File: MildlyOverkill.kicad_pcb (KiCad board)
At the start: 4 copper layers, 195 x 124 mm, 149 parts, among them J1 USB_C_Receptacle_USB2.0_16P, J2 2604-1102, J3 2604-1104, J4 2604-1104, J5 Conn_01x04_Pin, J6 Conn_01x04_MountingPin, J7 Conn_01x04_Pin, Q10 BTN8982TA, Q5 QM6015D, Q7 BTN8982TA, Q8 BTN8982TA, Q9 BTN8982TA, U1 ESP32-S3-WROOM-1, U2 MCP3208, U3 LD1117S33TR_SOT223, U4 TPS4H160AQPWPRQ1, U5 USBLC6-2P6, U6 TPS62932

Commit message: Added ethernet and ntcs
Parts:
- added C15: 1.5nF, Capacitor_SMD:C_0603_1608Metric, F.Cu at (27.5, 125.4)
- added C18: 1.5nF, Capacitor_SMD:C_0603_1608Metric, F.Cu at (39.5, 125.4)
- added C19: 1.5nF, Capacitor_SMD:C_0603_1608Metric, F.Cu at (33.5, 125.4)
- added C20: 1.5nF, Capacitor_SMD:C_0603_1608Metric, F.Cu at (45.5, 125.4)
- added J8: RJ45_Wuerth_7499010211A, Connector_RJ:RJ45_Wuerth_7499010211A_Horizontal, F.Cu at (163.2, 59.4)
- added TH1: Thermistor_NTC, Resistor_SMD:R_0805_2012Metric_Pad1.20x1.40mm_HandSolder, F.Cu at (27.9, 114.8)
- added TH2: Thermistor_NTC, Resistor_SMD:R_0805_2012Metric_Pad1.20x1.40mm_HandSolder, F.Cu at (27.9, 117.7)
- added TH3: Thermistor_NTC, Resistor_SMD:R_0805_2012Metric_Pad1.20x1.40mm_HandSolder, F.Cu at (27.9, 120.7)
- added U7: W5500, Package_QFP:LQFP-48_7x7mm_P0.5mm, F.Cu at (158.5, 75.5)
- R14, R23, R8, R9: value 6k -> 33k
- R25, R26, R27, R28: value 3k -> 3.3k
- R57, R58, R59, R60: value 5.1k -> 0R; footprint Resistor_SMD:R_0805_2012Metric -> Resistor_SMD:R_0805_2012Metric_Pad1.20x1.40mm_HandSolder
- R64, R65, R67, R68, R69, R70, R71, R72: footprint Resistor_SMD:R_0603_1608Metric_Pad0.98x0.95mm_HandSolder -> Resistor_SMD:R_0805_2012Metric_Pad1.20x1.40mm_HandSolder
- moved J2 168.8 mm to (251.5, 54.2), turned to 180 degrees
- moved C16 155.5 mm to (255.0, 75.5)
- moved C10 133.3 mm to (55.5, 67.7)
- moved C11 133.3 mm to (48.5, 95.0)
- moved C12 133.3 mm to (52.0, 71.7)
- moved C13 133.3 mm to (45.5, 74.5)
- moved C14 133.3 mm to (41.5, 75.5)
- moved C5 133.3 mm to (57.0, 73.5)
- moved L1 133.3 mm to (56.5, 84.0)
- moved R55 133.3 mm to (53.5, 67.6)
- moved R56 133.3 mm to (51.5, 67.6)
- moved U6 133.3 mm to (48.5, 73.0)
- moved D22 110.1 mm to (51.5, 101.7), turned to 90 degrees
- moved J6 58.3 mm to (115.7, 74.7)
- moved U4 53.5 mm to (150.3, 130.8)
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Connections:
- D11 pad 1: Net-(D11-K) -> GND
- D11 pad 2: GND -> Net-(D11-A)
- D12 pad 1: Net-(D12-K) -> GND
- D12 pad 2: GND -> Net-(D12-A)
- D13 pad 1: Net-(D13-K) -> GND
- D13 pad 2: GND -> Net-(D13-A)
- D23 pad 1: Net-(D23-K) -> GND
- D23 pad 2: GND -> Net-(D23-A)
- R14 pad 2: Net-(D3-K) -> GPIO3
- R23 pad 2: Net-(D4-K) -> GPIO4
- R25 pad 1: Net-(D1-K) -> GPIO1
- R26 pad 1: Net-(D2-K) -> GPIO2
- R27 pad 1: Net-(D3-K) -> GPIO3
- R28 pad 1: Net-(D4-K) -> GPIO4
- R52 pad 2: Net-(D11-K) -> Net-(D11-A)
- R53 pad 2: Net-(D12-K) -> Net-(D12-A)
- R54 pad 2: Net-(D13-K) -> Net-(D13-A)
- R61 pad 2: Net-(D23-K) -> Net-(D23-A)
- R8 pad 2: Net-(D1-K) -> GPIO1
- R9 pad 2: Net-(D2-K) -> GPIO2
- U1 pad 31: LED2 -> ETH_CS
- U2 pad 5: unconnected-(U2-CH4-Pad5) -> NTC1
- U2 pad 6: unconnected-(U2-CH5-Pad6) -> NTC2
- U2 pad 7: unconnected-(U2-CH6-Pad7) -> NTC3
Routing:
- added copper zone on F.Cu, net GPIO1
- added copper zone on F.Cu, net GPIO2
- added copper zone on F.Cu, net GPIO3
- added copper zone on F.Cu, net GPIO4
- removed copper zone on F.Cu, net Net-(D1-K)
- removed copper zone on F.Cu, net Net-(D2-K)
- removed copper zone on F.Cu, net Net-(D3-K)
- removed copper zone on F.Cu, net Net-(D4-K)

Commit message: kinda finished high power i guess
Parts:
- removed D1, D2, D3, D4: 3v, Diode_SMD:D_SOD-123
- removed D24: 5V, LED_SMD:LED_0603_1608Metric
- added C21: 0.1uF, Capacitor_SMD:C_0603_1608Metric, F.Cu at (41.0, 3.27)
- added C26: 10uF 16V, Capacitor_THT:CP_Radial_D4.0mm_P2.00mm, F.Cu at (32.6, 16.5)
- added C27: 4.7uF, Capacitor_SMD:C_1206_3216Metric, F.Cu at (41.4, 46.8)
- added C28: 10nF, Capacitor_SMD:C_0805_2012Metric, F.Cu at (36.3, 26.6)
- added C29: 10nF, Capacitor_SMD:C_0805_2012Metric, F.Cu at (36.3, 29.6)
- added C30: 10nF, Capacitor_SMD:C_0805_2012Metric, F.Cu at (36.3, 32.6)
- added C31: 10nF, Capacitor_SMD:C_0805_2012Metric, F.Cu at (36.3, 35.6)
- added C32: 22nF, Capacitor_SMD:C_0805_2012Metric, F.Cu at (36.3, 38.6)
- added C33: 18pF, Capacitor_SMD:C_0805_2012Metric, F.Cu at (36.3, 41.7)
- added C34: 18pF, Capacitor_SMD:C_0805_2012Metric, F.Cu at (36.3, 44.7)
- added C35: 10uF 16V, Capacitor_THT:CP_Radial_D4.0mm_P2.00mm, F.Cu at (20.5, 52.0)
- added C36: 0.1uF, Capacitor_SMD:C_0603_1608Metric, F.Cu at (40.5, 62.0)
- added C37: 0.1uF, Capacitor_SMD:C_0603_1608Metric, F.Cu at (40.5, 64.5)
- added C38: 0.1uF, Capacitor_SMD:C_0603_1608Metric, F.Cu at (40.5, 67.0)
- added C39: 0.1uF, Capacitor_SMD:C_0603_1608Metric, F.Cu at (44.5, 57.0)
- added C40: 0.1uF, Capacitor_SMD:C_0603_1608Metric, F.Cu at (48.4, 59.7)
- added C41: 0.1uF, Capacitor_SMD:C_0603_1608Metric, F.Cu at (44.5, 62.0)
- added C42: 1nF 10kV, Capacitor_SMD:C_0805_2012Metric, F.Cu at (36.3, 47.7)
- added FB2: GZ2012D121TF, Inductor_SMD:L_0805_2012Metric, F.Cu at (2.27, 61.0)
- added H1: MountingHole, MountingHole:MountingHole_2.1mm, F.Cu at (183.5, 91.5)
- added H2: MountingHole, MountingHole:MountingHole_2.1mm, F.Cu at (258.2, 91.5)
- added H3: MountingHole, MountingHole:MountingHole_2.1mm, F.Cu at (258.2, 147.5)
- added H4: MountingHole, MountingHole:MountingHole_2.1mm, F.Cu at (183.5, 147.5)
- added M1: Fan_4pin, Connector:FanPinHeader_1x04_P2.54mm_Vertical, F.Cu at (143.0, 89.0)
- added R66: 10, Resistor_SMD:R_0805_2012Metric, F.Cu at (6.12, 36.1)
- added R73: 1M, Resistor_SMD:R_0805_2012Metric, F.Cu at (6.12, 39.0)
- added R74: 0, Capacitor_SMD:C_0603_1608Metric_Pad1.08x0.95mm_HandSolder, F.Cu at (6.92, 50.8)
- added R75: 330, Resistor_SMD:R_0805_2012Metric, F.Cu at (6.12, 42.0)
- added R76: 330, Resistor_SMD:R_0805_2012Metric, F.Cu at (10.5, 24.3)
- added R77: R, Resistor_SMD:R_0805_2012Metric, F.Cu at (250.2, 56.5)
- added R78: R, Resistor_SMD:R_0805_2012Metric, F.Cu at (250.2, 54.5)
- added R79: R, Resistor_SMD:R_0805_2012Metric, F.Cu at (250.2, 52.5)
- added Y1: 3134250001, Crystal:Crystal_SMD_3225-4Pin_3.2x2.5mm_HandSoldering, F.Cu at (41.9, 42.2)
- J7: value Conn_01x04_Pin -> Conn_01x02_Pin; footprint Connector_PinHeader_2.54mm:PinHeader_1x04_P2.54mm_Vertical -> Connector_PinHeader_2.54mm:PinHeader_1x02_P2.54mm_Vertical
- R40: value 10K -> 22K
- R41: value 1k -> 12.4K
- R42, R43: value 1k -> 82
- R44: value 1k -> 49
- R49: value 10K -> 39K
- R50: value 10K -> 82K
- R62: value 210 -> 49
- TH2: footprint Resistor_SMD:R_0805_2012Metric_Pad1.20x1.40mm_HandSolder -> Connector_PinHeader_2.54mm:PinHeader_1x02_P2.54mm_Vertical
- moved R42 280.4 mm to (1.71, 27.2), turned to 0 degrees
- moved R44 263.2 mm to (1.71, 33.1), turned to 0 degrees
- moved J4 255.7 mm to (-14.5, -51.7)
- moved C18 228.6 mm to (268.0, 133.3), turned to 180 degrees
- moved C20 222.8 mm to (268.0, 113.3), turned to 180 degrees
- moved R72 213.9 mm to (15.1, 33.1)
- moved R69 213.6 mm to (15.1, 27.2)
- moved R70 213.5 mm to (15.1, 30.2)
- moved R65 212.9 mm to (15.1, 24.3)
- moved TH1 208.9 mm to (234.0, 81.0), turned to 90 degrees
- moved R43 198.0 mm to (1.71, 30.2), turned to 0 degrees
- moved R41 195.6 mm to (1.71, 24.3), turned to 0 degrees
- moved JP9 182.5 mm to (42.0, 37.6)
- moved JP6 181.7 mm to (42.0, 30.5)
- moved JP7 181.7 mm to (42.0, 34.0)
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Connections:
- R40 pad 1: ~{ST2} -> Net-(U4-~{ST2})
- R40 pad 2: +3.3V -> ST
- R41 pad 1: Net-(D1-K) -> Net-(U7-EXRES1)
- R41 pad 2: GPIO1 -> GND
- R42 pad 1: Net-(D2-K) -> Net-(U7-RXP)
- R42 pad 2: GPIO2 -> Net-(J8-CRD)
- R43 pad 1: Net-(D3-K) -> Net-(U7-RXN)
- R43 pad 2: GPIO3 -> Net-(J8-CRD)
- R44 pad 1: Net-(D4-K) -> +3.3VA
- R44 pad 2: GPIO4 -> Net-(J8-TD+)
- R49 pad 1: ~{ST3} -> Net-(U4-~{ST3})
- R49 pad 2: +3.3V -> ST
- R50 pad 1: ~{ST4} -> Net-(U4-~{ST4})
- R50 pad 2: +3.3V -> ST
- R62 pad 1: LED2 -> +3.3VA
- R62 pad 2: Net-(D24-K) -> Net-(J8-TD-)
- R7 pad 1: +3.3V -> Net-(U4-~{ST1})
- R7 pad 2: ~{ST1} -> ST
- U1 pad 16: Net-(J7-Pin_3) -> Net-(M1-PWM)
- U1 pad 26: Net-(J7-Pin_4) -> Net-(M1-Tacho)
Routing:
- net IS3: track 27.0 -> 183.8 mm
- net IS1: track 27.0 -> 153.6 mm
- net IS2: track 27.0 -> 119.1 mm
- net IS4: track 27.0 -> 92.5 mm
- net NTC1: track 0.00 -> 41.2 mm, vias 0 -> 2
- net VCC: track 12.9 -> 49.7 mm, vias 0 -> 202
- net Net-(D22-A): track 30.3 -> 0.00 mm, vias 2 -> 0
- net GPIO1: track 21.3 -> 36.4 mm, vias 0 -> 2
- net GND: track 16.7 -> 30.1 mm, vias 201 -> 294
- net GPIO4: track 50.3 -> 37.1 mm, vias 1 -> 2
- net GPIO2: track 21.3 -> 8.09 mm, vias 0 -> 1
- net GPIO3: track 21.3 -> 9.59 mm, vias 0 -> 1
- net Net-(U6-FB): track 9.04 -> 0.00 mm
- net Net-(D9-A): track 0.00 -> 8.29 mm
- net Net-(U6-BST): track 7.09 -> 0.00 mm
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- added copper zone on B.Cu, net (none)
- added copper zone on In2.Cu, net GND
- added copper zone on B.Cu, net IO1
- added copper zone on B.Cu, net IO2
- added copper zone on B.Cu, net IO3
- added copper zone on B.Cu, net IO4
- added copper zone on B.Cu, net Net-(J2-1_1)
- added copper zone on F.Cu, net Net-(J2-1_1)
- added copper zone on B.Cu, net VCC
- removed copper zone on B.Cu, net GND
- removed copper zone on F.Cu, net GPIO1
- removed copper zone on F.Cu, net GPIO2
- removed copper zone on F.Cu, net GPIO3
- removed copper zone on F.Cu, net GPIO4

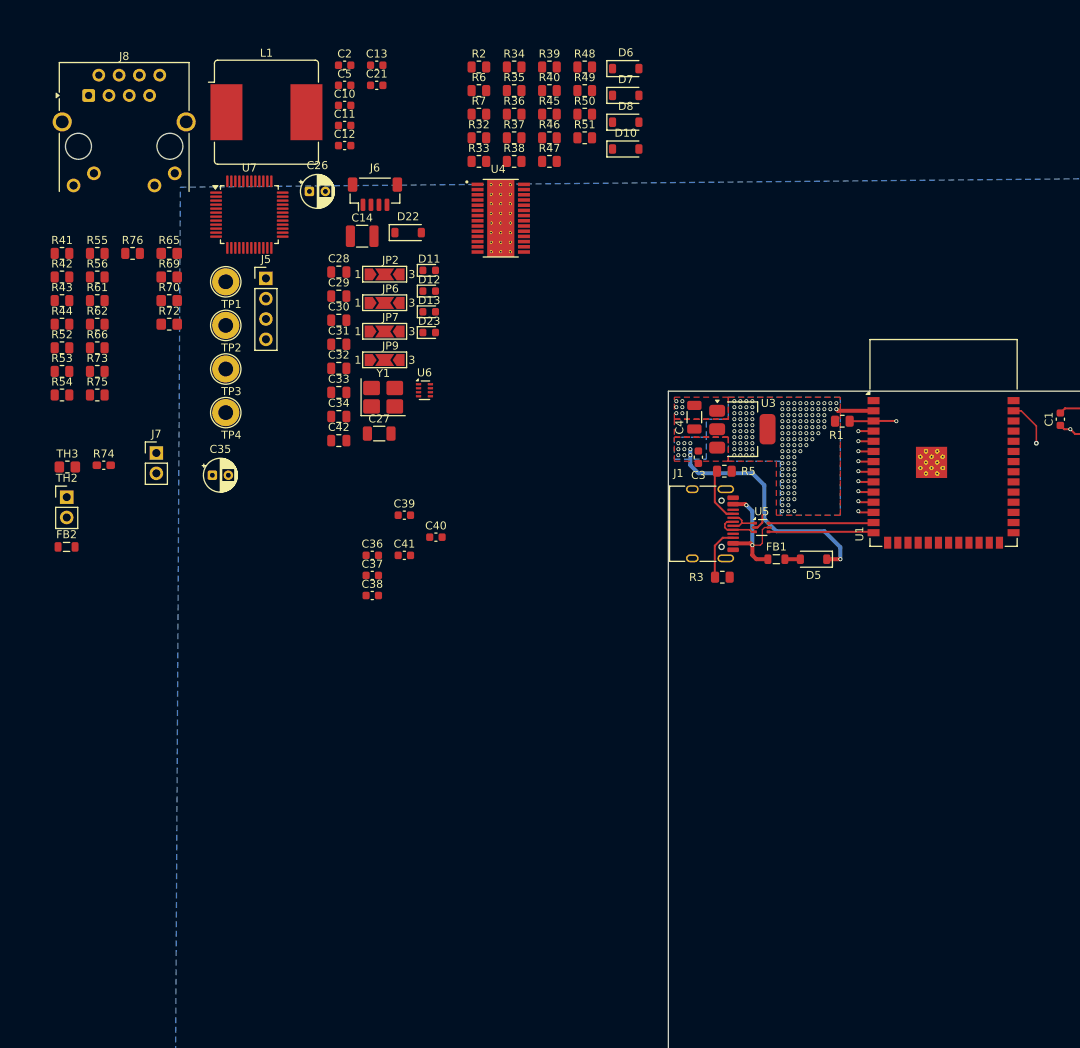
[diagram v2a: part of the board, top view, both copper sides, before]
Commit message: updated gitignore, ainteractive BOM and not much else
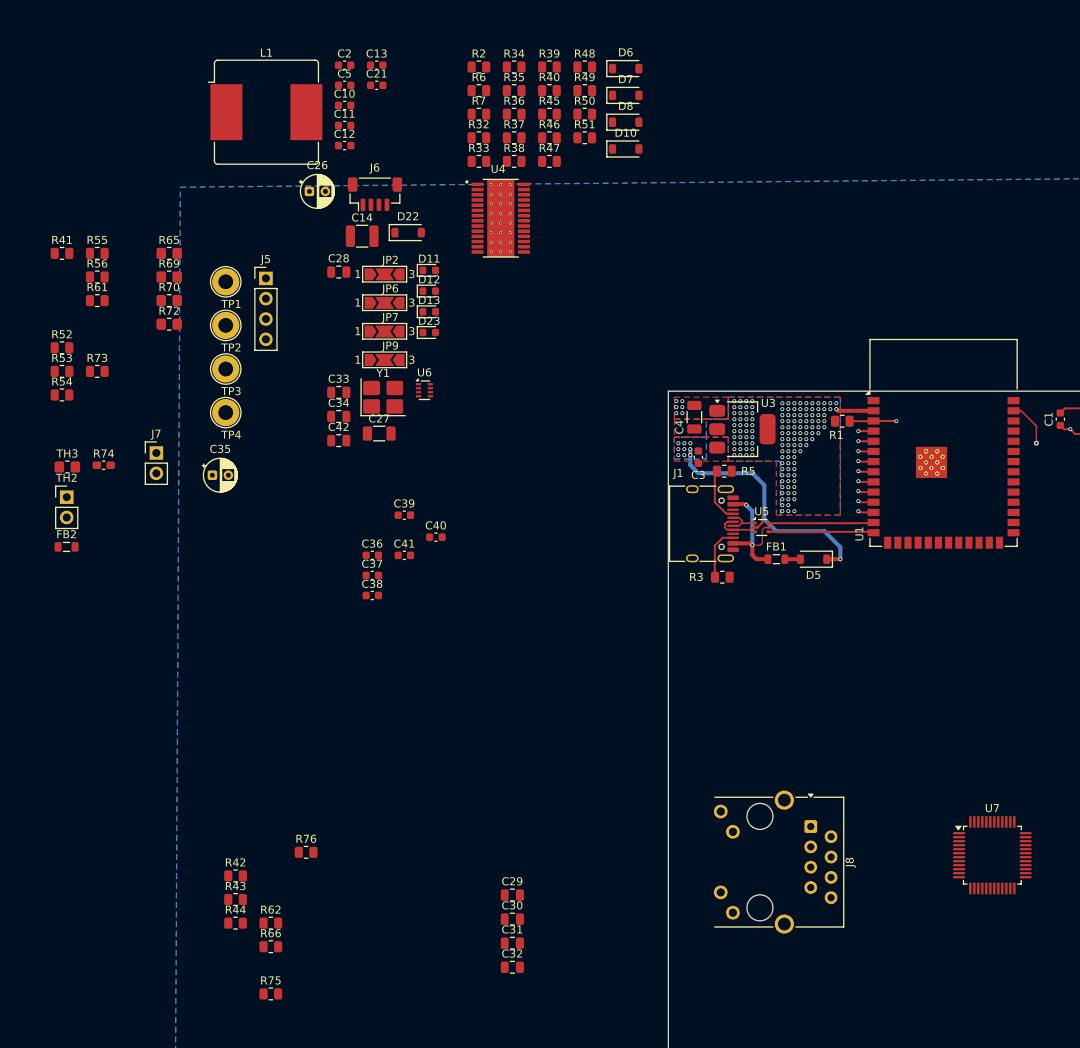
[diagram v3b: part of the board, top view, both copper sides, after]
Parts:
- moved J8 128.4 mm to (95.3, 95.9), turned to -90 degrees
- moved U7 122.6 mm to (118.0, 99.5)
- moved C29 77.9 mm to (58.0, 104.5)
- moved C31 77.9 mm to (58.0, 110.5)
- moved C32 77.9 mm to (58.0, 113.5)
- moved R42 77.9 mm to (23.4, 102.1)
- moved R43 77.9 mm to (23.4, 105.0)
- moved R75 77.9 mm to (27.8, 116.8)
- moved R76 77.9 mm to (32.2, 99.1)
- moved C30 77.9 mm to (58.0, 107.5)
- moved R44 77.9 mm to (23.4, 108.0)
- moved R62 77.9 mm to (27.8, 108.0)
- moved R66 77.9 mm to (27.8, 110.9)

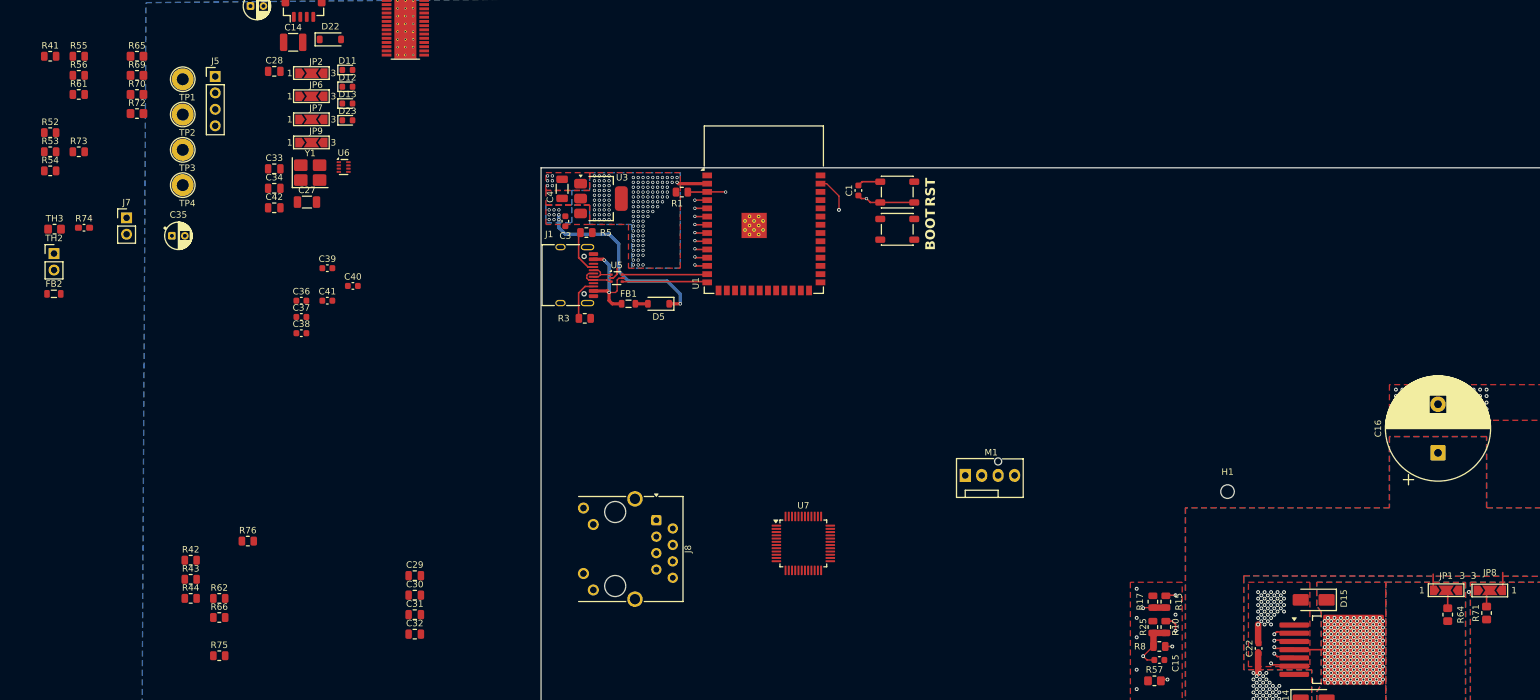
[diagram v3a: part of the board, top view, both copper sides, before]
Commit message: routed ethernet
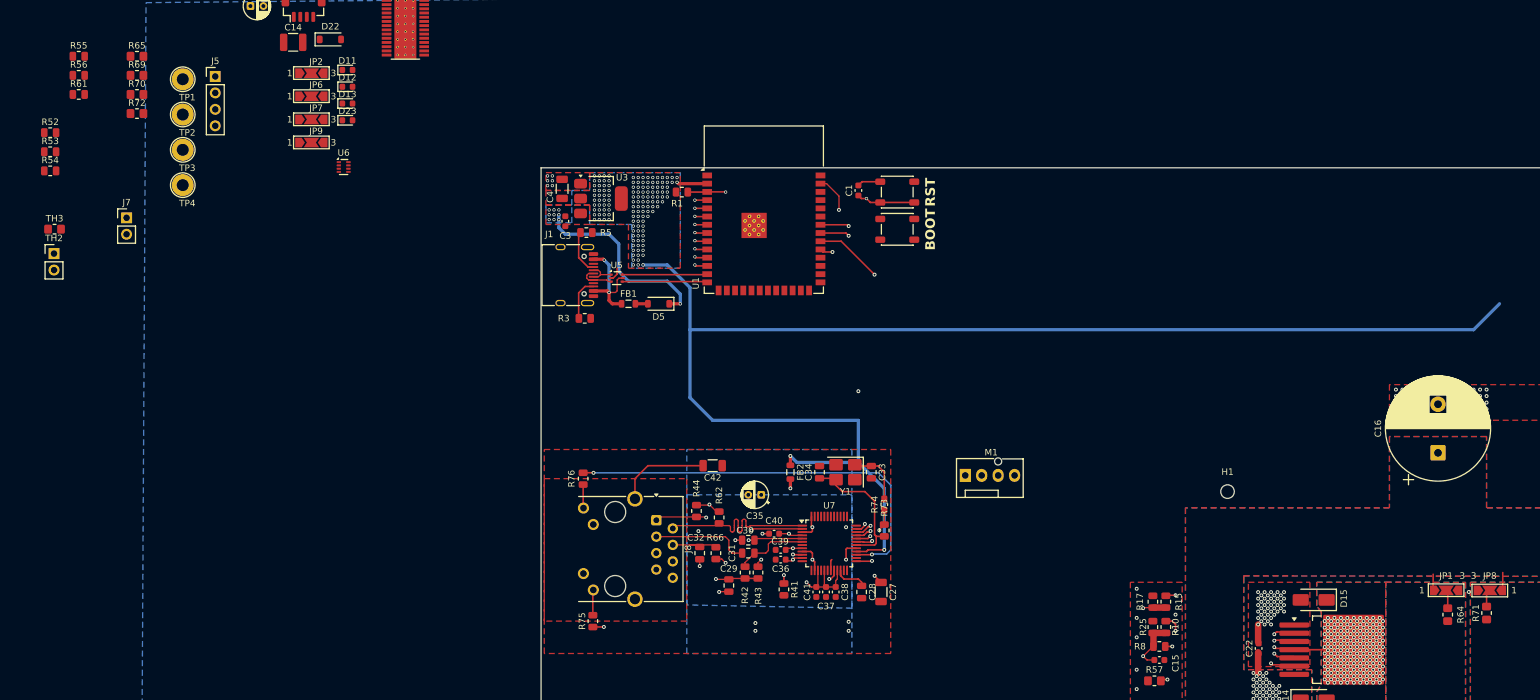
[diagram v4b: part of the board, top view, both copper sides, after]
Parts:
- C42: footprint Capacitor_SMD:C_0805_2012Metric -> Capacitor_SMD:C_1206_3216Metric
- moved R41 140.0 mm to (115.0, 106.6), turned to -90 degrees
- moved R73 137.4 mm to (130.5, 97.5), turned to -90 degrees
- moved R74 130.8 mm to (130.5, 93.5), turned to -90 degrees
- moved C28 121.2 mm to (127.0, 107.0), turned to -90 degrees
- moved FB2 117.0 mm to (116.0, 88.5), turned to -90 degrees
- moved C27 107.2 mm to (130.0, 107.0), turned to -90 degrees
- moved C33 103.4 mm to (128.5, 88.5), turned to -90 degrees
- moved C35 99.4 mm to (111.5, 92.0), turned to 180 degrees
- moved C34 94.9 mm to (120.5, 88.5), turned to 90 degrees
- moved Y1 94.7 mm to (124.5, 88.5), turned to 180 degrees
- moved C38 91.7 mm to (123.0, 107.0), turned to -90 degrees
- moved C37 91.5 mm to (121.5, 107.0), turned to -90 degrees
- moved C41 87.9 mm to (120.0, 107.0), turned to -90 degrees
- moved R43 87.6 mm to (111.0, 104.0), turned to -90 degrees
- moved R42 85.6 mm to (109.0, 104.0), turned to -90 degrees
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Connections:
- net Net-(C42-Pad2) renamed /shield
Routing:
- net +3.3V: track 4.73 -> 223.0 mm, vias 135 -> 137
- net ETH_CS: track 0.00 -> 65.7 mm, vias 0 -> 2
- net ACT_LED: track 0.00 -> 63.9 mm, vias 0 -> 2
- net LINK_LED: track 0.00 -> 57.4 mm, vias 0 -> 2
- net MISO: track 0.00 -> 54.7 mm, vias 0 -> 2
- net SCLK: track 0.00 -> 52.9 mm, vias 0 -> 2
- net MOSI: track 0.00 -> 51.8 mm, vias 0 -> 2
- net +3.3VA: track 0.00 -> 29.1 mm, vias 0 -> 7
- net Net-(J8-TD-): track 0.00 -> 27.4 mm
- net Net-(J8-TD+): track 0.00 -> 24.6 mm, vias 0 -> 2
- net Net-(U7-XI/CLKIN): track 0.00 -> 21.5 mm
- net Net-(J8-CRD): track 0.00 -> 19.9 mm, vias 0 -> 1
- net GND: track 30.1 -> 47.1 mm, vias 294 -> 307
- net Net-(J8-RD+): track 0.00 -> 15.2 mm
- net /shield: track 0.00 -> 14.5 mm
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- added copper zone on B.Cu, net +3.3VA
- added copper zone on F.Cu, net /shield
